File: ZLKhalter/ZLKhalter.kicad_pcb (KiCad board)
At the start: 2 copper layers, 43.2 x 35.6 mm, 4 parts, among them J1 Conn_02x04_Counter_Clockwise, J2 Conn_01x04_Pin, J3 Conn_02x04_Counter_Clockwise

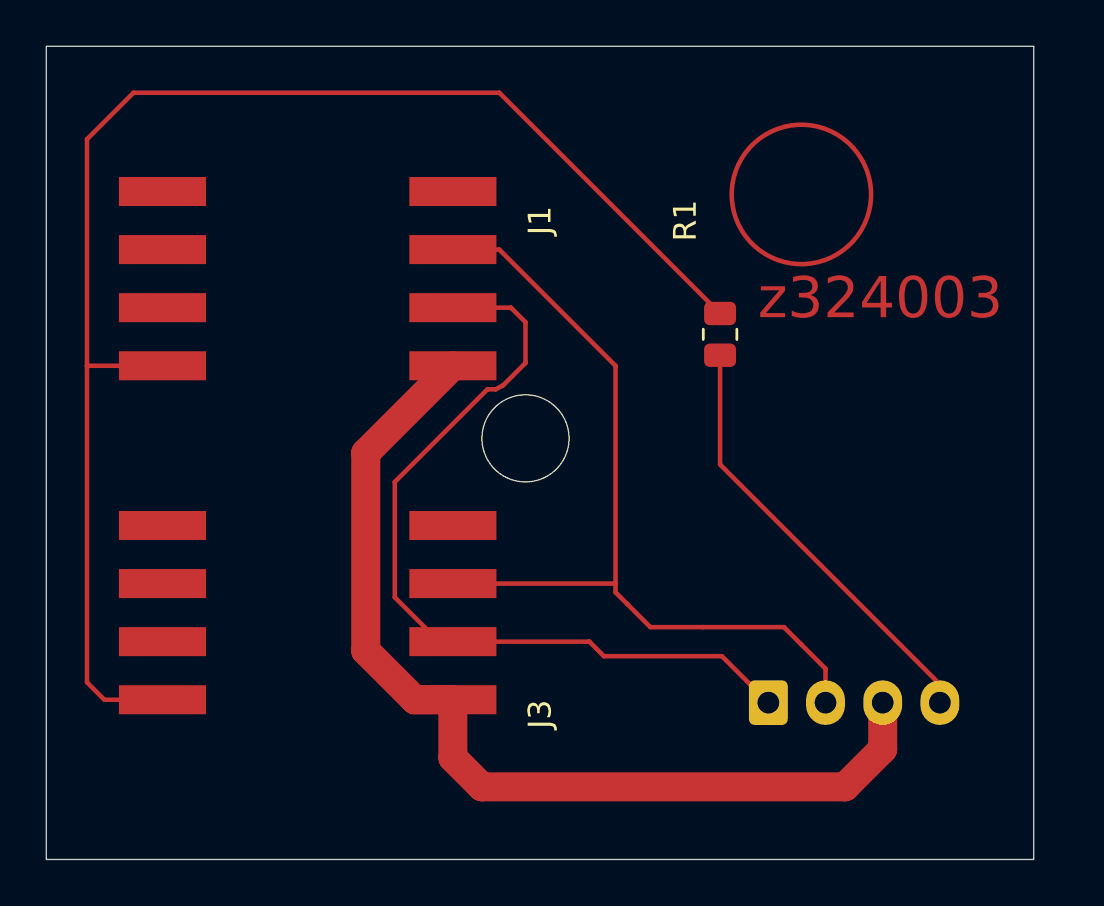
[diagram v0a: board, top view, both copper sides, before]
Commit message: kleinerer sim kontakt
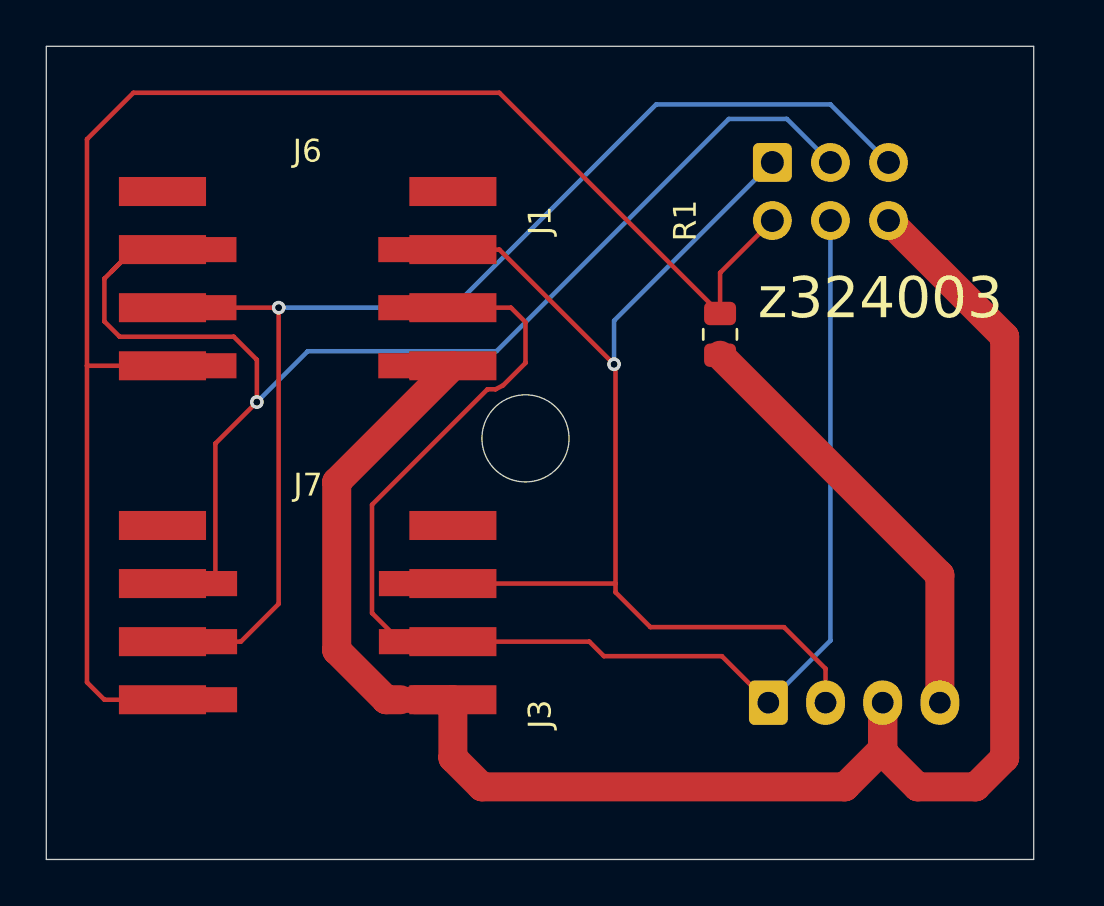
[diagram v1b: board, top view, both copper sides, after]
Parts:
- added J4: Conn_02x03_Odd_Even, Connector_IDC:IDC-Header_2x03_P2.54mm_Vertical, B.Cu at (142.2, 134.6)
- added J6: Conn_02x03_Top_Bottom, SIM:4FF-SIM, F.Cu at (121.9, 134.6)
- added J7: Conn_02x03_Top_Bottom, SIM:4FF-SIM, F.Cu at (121.9, 149.2)
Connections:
- net CLK renamed MISO
- net IO renamed MOSI
- J1 pad 6: unconnected-(J1-Pin_6-Pad6) -> SCK
- J1 pad 7: unconnected-(J1-Pin_7-Pad7) -> RST
- J3 pad 6: unconnected-(J3-Pin_6-Pad6) -> SCK
- J3 pad 7: unconnected-(J3-Pin_7-Pad7) -> RST
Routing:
- net SCK: track 0.00 -> 56.4 mm, vias 0 -> 1
- net RST: track 0.00 -> 55.2 mm, vias 0 -> 1
- net GND: track 43.3 -> 78.7 mm
- net MOSI: track 37.6 -> 60.0 mm
- net MISO: track 39.6 -> 51.2 mm, vias 0 -> 1
- net VCC: track 64.5 -> 69.5 mm

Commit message: 12v zlk
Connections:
- net Net-(J2-Pin_4) renamed +12V

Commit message: zlk widerstand
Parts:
- R1: value R -> 270; footprint Resistor_SMD:R_0805_2012Metric -> Resistor_SMD:R_0603_1608Metric_Pad0.98x0.95mm_HandSolder
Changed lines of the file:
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@@
 	(net 10 "unconnected-(J3-Pin_5-Pad5)")
 	(net 11 "+12V")
-	(footprint "Resistor_SMD:R_0805_2012Metric"
+	(footprint "Resistor_SMD:R_0603_1608Metric_Pad0.98x0.95mm_HandSolder"
 		(layer "F.Cu")
 		(at 139.954 142.1365 90)
-		(descr "Resistor SMD 0805 (2012 Metric), square (rectangular) end terminal, IPC_7351 nominal, (Body size source: IPC-SM-782 page 72, https://www.pcb-3d.com/wordpress/wp-content/uploads/ipc-sm-782a_amendment_1_and_2.pdf), generated with kicad-footprint-generator")
-		(tags "resistor")
+		(descr "Resistor SMD 0603 (1608 Metric), square (rectangular) end terminal, IPC-7351 nominal with elongated pad for handsoldering. (Body size source: IPC-SM-782 page 72, https://www.pcb-3d.com/wordpress/wp-content/uploads/ipc-sm-782a_amendment_1_and_2.pdf), generated with kicad-footprint-generator")
+		(tags "resistor handsolder")
 		(property "Reference" "R1"
-			(at 4.9765 -1.524 90)
+			(at 0 -1.43 90)
 			(layer "F.SilkS")
 			(effects
@@
 			)
 		)
-		(property "Value" "R"
-			(at 0 1.65 90)
+		(property "Value" "270"
+			(at 0 1.43 90)
 			(layer "F.Fab")
 			(effects
@@
 		(property "Datasheet" ""
 			(at 0 0 90)
-			(unlocked yes)
 			(layer "F.Fab")
 			(hide yes)
@@
 		(property "Description" "Resistor"
 			(at 0 0 90)
-			(unlocked yes)
-			(layer "F.Fab")
+			(layer "F.Fab")
+			(hide yes)
+			(effects
+				(font
+					(size 1.27 1.27)
+					(thickness 0.15)
+				)
+			)
+		)
+		(property "LCSC" "C22966"
+			(at 0 0 0)
+			(layer "F.SilkS")
 			(hide yes)
 			(effects
@@
 		(attr smd)
 		(fp_line
-			(start -0.227064 -0.735)
-			(end 0.227064 -0.735)
+			(start -0.254724 -0.5225)
+			(end 0.254724 -0.5225)
 			(stroke
 				(width 0.12)
@@
 		)
 		(fp_line
-			(start -0.227064 0.735)
-			(end 0.227064 0.735)
+			(start -0.254724 0.5225)
+			(end 0.254724 0.5225)
 			(stroke
 				(width 0.12)
@@
 		)
 		(fp_line
-			(start 1.68 -0.95)
-			(end 1.68 0.95)
+			(start 1.65 -0.73)
+			(end 1.65 0.73)
 			(stroke
 				(width 0.05)
@@
 		)
 		(fp_line
-			(start -1.68 -0.95)
-			(end 1.68 -0.95)
+			(start -1.65 -0.73)
+			(end 1.65 -0.73)
 			(stroke
 				(width 0.05)
@@
 		)
 		(fp_line
-			(start 1.68 0.95)
-			(end -1.68 0.95)
+			(start 1.65 0.73)
+			(end -1.65 0.73)
 			(stroke
 				(width 0.05)
@@
 		)
 		(fp_line
-			(start -1.68 0.95)
-			(end -1.68 -0.95)
+			(start -1.65 0.73)
+			(end -1.65 -0.73)
 			(stroke
 				(width 0.05)
@@
 		)
 		(fp_line
-			(start 1 -0.625)
-			(end 1 0.625)
-			(stroke
-				(width 0.1)
-				(type solid)
-			)
-			(layer "F.Fab")
-		)
-		(fp_line
-			(start -1 -0.625)
-			(end 1 -0.625)
-			(stroke
-				(width 0.1)
-				(type solid)
-			)
-			(layer "F.Fab")
-		)
-		(fp_line
-			(start 1 0.625)
-			(end -1 0.625)
-			(stroke
-				(width 0.1)
-				(type solid)
-			)
-			(layer "F.Fab")
-		)
-		(fp_line
-			(start -1 0.625)
-			(end -1 -0.625)
+			(start 0.8 -0.4125)
+			(end 0.8 0.4125)
+			(stroke
+				(width 0.1)
+				(type solid)
+			)
+			(layer "F.Fab")
+		)
+		(fp_line
+			(start -0.8 -0.4125)
+			(end 0.8 -0.4125)
+			(stroke
+				(width 0.1)
+				(type solid)
+			)
+			(layer "F.Fab")
+		)
+		(fp_line
+			(start 0.8 0.4125)
+			(end -0.8 0.4125)
+			(stroke
+				(width 0.1)
+				(type solid)
+			)
+			(layer "F.Fab")
+		)
+		(fp_line
+			(start -0.8 0.4125)
+			(end -0.8 -0.4125)
 			(stroke
 				(width 0.1)
@@
 			(effects
 				(font
-					(size 0.5 0.5)
-					(thickness 0.08)
+					(size 0.4 0.4)
+					(thickness 0.06)
 				)
 			)
@@
 		(pad "1" smd roundrect
 			(at -0.9125 0 90)
-			(size 1.025 1.4)
-			(layers "F.Cu" "F.Mask" "F.Paste")
-			(roundrect_rratio 0.243902)
+			(size 0.975 0.95)
+			(layers "F.Cu" "F.Mask" "F.Paste")
+			(roundrect_rratio 0.25)
 			(net 11 "+12V")
 			(pintype "passive")
@@
 		(pad "2" smd roundrect
 			(at 0.9125 0 90)
-			(size 1.025 1.4)
-			(layers "F.Cu" "F.Mask" "F.Paste")
-			(roundrect_rratio 0.243902)
+			(size 0.975 0.95)
+			(layers "F.Cu" "F.Mask" "F.Paste")
+			(roundrect_rratio 0.25)
 			(net 2 "VCC")
 			(pintype "passive")
 		)
 		(embedded_fonts no)
-		(model "${KICAD8_3DMODEL_DIR}/Resistor_SMD.3dshapes/R_0805_2012Metric.wrl"
+		(model "${KICAD9_3DMODEL_DIR}/Resistor_SMD.3dshapes/R_0603_1608Metric.wrl"
 			(offset
 				(xyz 0 0 0)
@@
 				(font
 					(size 1 1)
+					(thickness 0.15)
+				)
+			)
+		)
+		(property "LCSC" "C388791"
+			(at 0 0 0)
+			(layer "F.SilkS")
+			(hide yes)
+			(effects
+				(font
+					(size 1.27 1.27)
 					(thickness 0.15)
 				)
@@
 				(font
 					(size 1 1)
+					(thickness 0.15)
+				)
+			)
+		)
+		(property "LCSC" "C388791"
+			(at 0 0 0)
+			(layer "F.SilkS")
+			(hide yes)
+			(effects
+				(font
+					(size 1.27 1.27)
 					(thickness 0.15)
 				)
@@
 			)
 		)
+		(property "LCSC" "C7430309"
+			(at 0 0 0)
+			(layer "B.SilkS")
+			(hide yes)
+			(effects
+				(font
+					(size 1.27 1.27)
+					(thickness 0.15)
+				)
+			)
+		)
 		(property ki_fp_filters "Connector*:*_2x??_*")
 		(sheetname "/")
@@
 			)
 		)
+		(property "LCSC" "C157925"
+			(at 0 0 0)
+			(layer "B.SilkS")
+			(hide yes)
+			(effects
+				(font
+					(size 1.27 1.27)
+					(thickness 0.15)
+				)
+			)
+		)

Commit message: linie
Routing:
- net GND: track 78.7 -> 77.8 mm
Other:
- outline, holes or cut-outs redrawn
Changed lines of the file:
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@@
 		(at 121.934 149.225)
 		(property "Reference" "J7"
-			(at 0 -0.5 0)
+			(at -1.284 7.62 0)
 			(unlocked yes)
 			(layer "F.SilkS")
@@
 		(at 112.395 153.035 90)
 		(property "Reference" "J3"
-			(at -5.715 19.685 90)
+			(at -5.08 19.05 90)
 			(unlocked yes)
 			(layer "F.SilkS")
@@
 		(at 112.395 138.43 90)
 		(property "Reference" "J1"
-			(at 1.27 19.685 90)
+			(at 2.54 19.05 90)
 			(unlocked yes)
 			(layer "F.SilkS")
@@
 		(at 121.906 134.62)
 		(property "Reference" "J6"
-			(at 0 -0.5 0)
+			(at 1.284 4.445 0)
 			(unlocked yes)
 			(layer "F.SilkS")
@@
 		)
 	)
-	(gr_rect
-		(start 110.49 129.54)
-		(end 153.67 165.1)
+	(gr_line
+		(start 121.92 160.02)
+		(end 121.92 133.35)
 		(stroke
-			(width 0.05)
+			(width 0.1)
 			(type default)
 		)
-		(fill no)
-		(layer "Edge.Cuts")
+		(layer "F.SilkS")
 	)
 	(gr_circle
@@
 			(width 0.05)
 			(type default)
+		)
+		(fill no)
+		(layer "Edge.Cuts")
+	)
+	(gr_poly
+		(pts
+			(xy 153.67 129.54) (xy 110.49 129.54) (xy 110.744 165.1) (xy 153.416 165.1)
+		)
+		(stroke
+			(width 0.05)
+			(type solid)
 		)
 		(fill no)
@@
 	)
 	(segment
+		(start 148.59 161.925)
+		(end 150.495 161.925)
+		(width 1.27)
+		(layer "F.Cu")
+		(net 1)
+	)
+	(segment
 		(start 123.19 148.59)
 		(end 123.19 155.953)
@@
 	)
 	(segment
-		(start 151.13 161.925)
-		(end 152.4 160.655)
-		(width 1.27)
-		(layer "F.Cu")
-		(net 1)
-	)
-	(segment
 		(start 125.352 158.115)
 		(end 125.984 158.115)
@@
 	)
 	(segment
-		(start 152.4 142.24)
+		(start 151.765 141.605)
 		(end 147.32 137.16)
 		(width 1.27)
@@
 	)
 	(segment
+		(start 151.765 160.655)
+		(end 151.765 141.605)
+		(width 1.27)
+		(layer "F.Cu")
+		(net 1)
+	)
+	(segment
 		(start 147.066 160.401)
 		(end 148.59 161.925)
+		(width 1.27)
+		(layer "F.Cu")
+		(net 1)
+	)
+	(segment
+		(start 145.415 161.925)
+		(end 129.54 161.925)
+		(width 1.27)
+		(layer "F.Cu")
+		(net 1)
+	)
+	(segment
+		(start 123.19 155.953)
+		(end 125.352 158.115)
 		(width 1.27)
 		(layer "F.Cu")
@@
 	)
 	(segment
-		(start 145.415 161.925)
-		(end 129.54 161.925)
-		(width 1.27)
-		(layer "F.Cu")
-		(net 1)
-	)
-	(segment
-		(start 123.19 155.953)
-		(end 125.352 158.115)
-		(width 1.27)
-		(layer "F.Cu")
-		(net 1)
-	)
-	(segment
 		(start 128.27 143.51)
 		(end 123.19 148.59)
@@
 	)
 	(segment
-		(start 148.59 161.925)
-		(end 151.13 161.925)
+		(start 150.495 161.925)
+		(end 151.765 160.655)
 		(width 1.27)
 		(layer "F.Cu")
-		(net 1)
-	)
-	(segment
-		(start 152.4 160.655)
-		(end 152.4 142.24)
-		(width 1.27)
-		(layer "F.Cu")

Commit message: halter sid sod
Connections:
- net MISO renamed SID_MISO
- net MOSI renamed SOD_MOSI
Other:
- board text added: "Supposed to be angled"
